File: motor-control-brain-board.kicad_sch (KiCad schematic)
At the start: 35 parts, among them J1 GPIO, J10 PWM, J11 PWR, J12 POWER_SENSE, J13 MISC_SENSE, J2 I2C, J3 SERIAL_1, J4 SERIAL_2, J5 CAN, J6 SPI, J7 USB_C_Receptacle_USB2.0_16P, J8 SWD, J9 POS_SENSE, SW1 RST, U1 TLV76750QWDRBxQ1, U2 TLV76733QWDRBxQ1

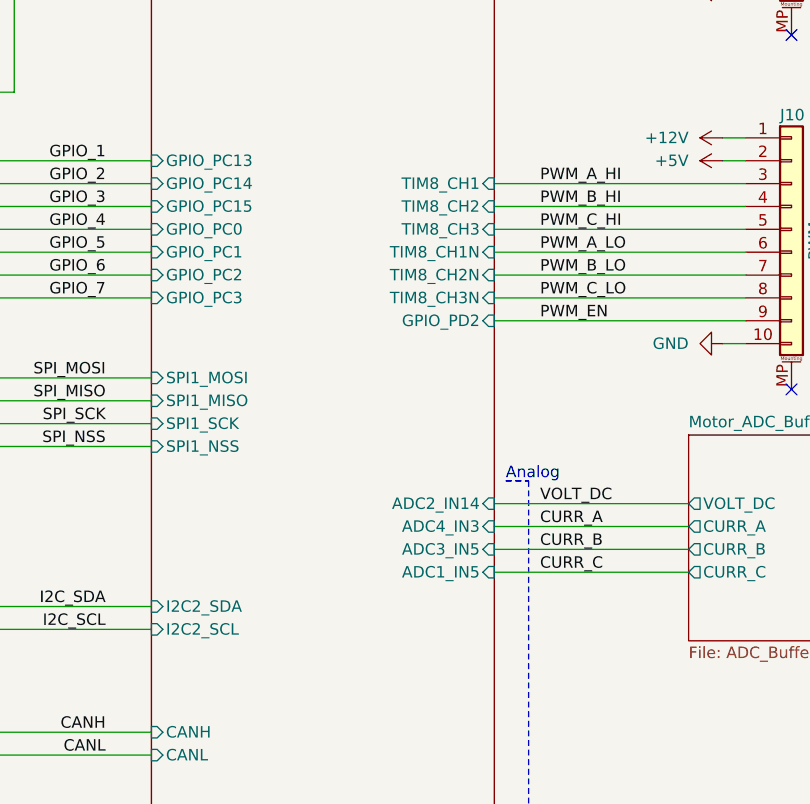
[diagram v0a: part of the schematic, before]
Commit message: Updated schematic to use HRTIM1 and reviewed
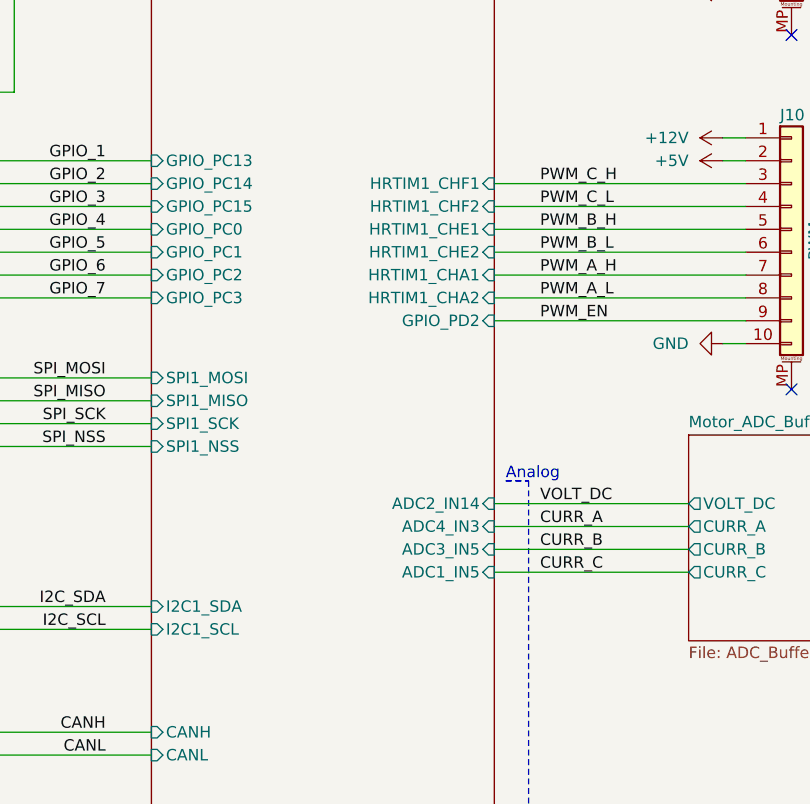
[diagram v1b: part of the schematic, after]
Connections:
- net PWM_A_HI renamed PWM_C_H
- net PWM_A_LO renamed PWM_B_L
- net PWM_B_HI renamed PWM_C_L
- net PWM_B_LO renamed PWM_A_H
- net PWM_C_HI renamed PWM_B_H
- net PWM_C_LO renamed PWM_A_L
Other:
- sheet MCU ports: added HRTIM1_CHA1, HRTIM1_CHA2, HRTIM1_CHE1, HRTIM1_CHE2, HRTIM1_CHF1, HRTIM1_CHF2, I2C1_SCL, I2C1_SDA; removed I2C2_SCL, I2C2_SDA, TIM8_CH1, TIM8_CH1N, TIM8_CH2, TIM8_CH2N, TIM8_CH3, TIM8_CH3N
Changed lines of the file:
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@@
 	(wire
 		(pts
+			(xy 137.16 78.74) (xy 165.1 78.74)
+		)
+		(stroke
+			(width 0)
+			(type default)
+		)
+	)
+	(wire
+		(pts
 			(xy 74.93 29.21) (xy 83.82 29.21)
 		)
@@
 	(wire
 		(pts
-			(xy 137.16 81.28) (xy 165.1 81.28)
-		)
-		(stroke
-			(width 0)
-			(type default)
-		)
-	)
-	(wire
-		(pts
 			(xy 74.93 21.59) (xy 81.28 21.59)
 		)
@@
 	(wire
 		(pts
+			(xy 137.16 86.36) (xy 165.1 86.36)
+		)
+		(stroke
+			(width 0)
+			(type default)
+		)
+	)
+	(wire
+		(pts
 			(xy 208.28 38.1) (xy 208.28 39.37)
 		)
@@
 		)
 	)
-	(wire
-		(pts
-			(xy 137.16 86.36) (xy 165.1 86.36)
-		)
-		(stroke
-			(width 0)
-			(type default)
-		)
-	)
 	(polyline
 		(pts
@@
 	(wire
 		(pts
-			(xy 137.16 78.74) (xy 165.1 78.74)
-		)
-		(stroke
-			(width 0)
-			(type default)
-		)
-	)
-	(wire
-		(pts
 			(xy 137.16 83.82) (xy 165.1 83.82)
 		)
@@
 	(wire
 		(pts
+			(xy 137.16 81.28) (xy 165.1 81.28)
+		)
+		(stroke
+			(width 0)
+			(type default)
+		)
+	)
+	(wire
+		(pts
 			(xy 137.16 71.12) (xy 165.1 71.12)
 		)
@@
 		)
 	)
-	(label "PWM_B_LO"
+	(label "PWM_A_H"
 		(at 142.24 81.28 0)
 		(effects
@@
 		)
 	)
-	(label "PWM_A_HI"
+	(label "PWM_C_H"
 		(at 142.24 71.12 0)
 		(effects
@@
 		)
 	)
-	(label "PWM_C_LO"
+	(label "PWM_A_L"
 		(at 142.24 83.82 0)
 		(effects
@@
 		)
 	)
-	(label "PWM_C_HI"
+	(label "PWM_B_H"
 		(at 142.24 76.2 0)
 		(effects
@@
 		)
 	)
-	(label "PWM_A_LO"
+	(label "PWM_B_L"
 		(at 142.24 78.74 0)
 		(effects
@@
 		)
 	)
-	(label "PWM_B_HI"
+	(label "PWM_C_L"
 		(at 142.24 73.66 0)
 		(effects
@@
 			)
 		)
-		(pin "TIM8_CH2N" input
-			(at 137.16 81.28 0)
-			(effects
-				(font
-					(size 1.27 1.27)
-				)
-				(justify right)
-			)
-		)
-		(pin "TIM8_CH1N" input
-			(at 137.16 78.74 0)
-			(effects
-				(font
-					(size 1.27 1.27)
-				)
-				(justify right)
-			)
-		)
-		(pin "TIM8_CH3N" input
-			(at 137.16 83.82 0)
-			(effects
-				(font
-					(size 1.27 1.27)
-				)
-				(justify right)
-			)
-		)
 		(pin "GPIO_PC15" input
 			(at 99.06 73.66 180)
@@
 			)
 		)
-		(pin "TIM8_CH3" input
-			(at 137.16 76.2 0)
-			(effects
-				(font
-					(size 1.27 1.27)
-				)
-				(justify right)
-			)
-		)
 		(pin "GPIO_PC2" input
 			(at 99.06 81.28 180)
@@
 			)
 		)
-		(pin "TIM8_CH2" input
-			(at 137.16 73.66 0)
-			(effects
-				(font
-					(size 1.27 1.27)
-				)
-				(justify right)
-			)
-		)
-		(pin "TIM8_CH1" input
-			(at 137.16 71.12 0)
-			(effects
-				(font
-					(size 1.27 1.27)
-				)
-				(justify right)
-			)
-		)
 		(pin "GPIO_PC0" input
 			(at 99.06 76.2 180)
@@
 			)
 		)
-		(pin "I2C2_SDA" input
-			(at 99.06 118.11 180)
-			(effects
-				(font
-					(size 1.27 1.27)
-				)
-				(justify left)
-			)
-		)
-		(pin "I2C2_SCL" input
-			(at 99.06 120.65 180)
-			(effects
-				(font
-					(size 1.27 1.27)
-				)
-				(justify left)
-			)
-		)
 		(pin "USB_DM" input
 			(at 99.06 44.45 180)
@@
 			)
 		)
+		(pin "HRTIM1_CHE2" input
+			(at 137.16 78.74 0)
+			(effects
+				(font
+					(size 1.27 1.27)
+				)
+				(justify right)
+			)
+		)
+		(pin "I2C1_SDA" input
+			(at 99.06 118.11 180)
+			(effects
+				(font
+					(size 1.27 1.27)
+				)
+				(justify left)
+			)
+		)
+		(pin "I2C1_SCL" input
+			(at 99.06 120.65 180)
+			(effects
+				(font
+					(size 1.27 1.27)
+				)
+				(justify left)
+			)
+		)
+		(pin "HRTIM1_CHA1" input
+			(at 137.16 81.28 0)
+			(effects
+				(font
+					(size 1.27 1.27)
+				)
+				(justify right)
+			)
+		)
+		(pin "HRTIM1_CHA2" input
+			(at 137.16 83.82 0)
+			(effects
+				(font
+					(size 1.27 1.27)
+				)
+				(justify right)
+			)
+		)
+		(pin "HRTIM1_CHE1" input
+			(at 137.16 76.2 0)
+			(effects
+				(font
+					(size 1.27 1.27)
+				)
+				(justify right)
+			)
+		)
+		(pin "HRTIM1_CHF1" input
+			(at 137.16 71.12 0)
+			(effects
+				(font
+					(size 1.27 1.27)
+				)
+				(justify right)
+			)
+		)
+		(pin "HRTIM1_CHF2" input
+			(at 137.16 73.66 0)
+			(effects
+				(font
+					(size 1.27 1.27)
+				)
+				(justify right)
+			)
+		)
 		(instances
-			(project "Motor_Control_Brain_Board"
+			(project "motor-control-brain-board"
 				(path "/7261d109-8405-40e9-921c-d95f374a7164"
 					(page "2")
@@
 		)
 		(instances
-			(project "Motor_Control_Brain_Board"
+			(project "motor-control-brain-board"
 				(path "/7261d109-8405-40e9-921c-d95f374a7164"
 					(page "4")
@@
 		)
 		(instances
-			(project "Motor_Control_Brain_Board"
+			(project "motor-control-brain-board"
 				(path "/7261d109-8405-40e9-921c-d95f374a7164"
 					(page "3")

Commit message: Routed Stuff
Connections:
- net CANH: now also J5.3 (Pin_3); no longer J5.2 (Pin_2)
- net CANL: now also J5.2 (Pin_2); no longer J5.3 (Pin_3)
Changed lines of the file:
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@@
 	(wire
 		(pts
+			(xy 60.96 134.62) (xy 99.06 134.62)
+		)
+		(stroke
+			(width 0)
+			(type default)
+		)
+	)
+	(wire
+		(pts
 			(xy 208.28 26.67) (xy 208.28 27.94)
 		)
@@
 	(wire
 		(pts
-			(xy 60.96 134.62) (xy 99.06 134.62)
-		)
-		(stroke
-			(width 0)
-			(type default)
-		)
-	)
-	(wire
-		(pts
 			(xy 191.77 106.68) (xy 217.17 106.68)
 		)
@@
 	(wire
 		(pts
+			(xy 60.96 132.08) (xy 99.06 132.08)
+		)
+		(stroke
+			(width 0)
+			(type default)
+		)
+	)
+	(wire
+		(pts
 			(xy 191.77 119.38) (xy 217.17 119.38)
 		)
@@
 	(wire
 		(pts
-			(xy 60.96 132.08) (xy 99.06 132.08)
-		)
-		(stroke
-			(width 0)
-			(type default)
-		)
-	)
-	(wire
-		(pts
 			(xy 242.57 64.77) (xy 234.95 64.77)
 		)
@@
 	)
 	(label "CANL"
-		(at 93.98 134.62 180)
+		(at 93.98 132.08 180)
 		(effects
 			(font
@@
 	)
 	(label "CANH"
-		(at 93.98 132.08 180)
+		(at 93.98 134.62 180)
 		(effects
 			(font
@@
 		)
 		(pin "CANH" input
-			(at 99.06 132.08 180)
+			(at 99.06 134.62 180)
 			(effects
 				(font
@@
 		)
 		(pin "CANL" input
-			(at 99.06 134.62 180)
+			(at 99.06 132.08 180)
 			(effects
 				(font

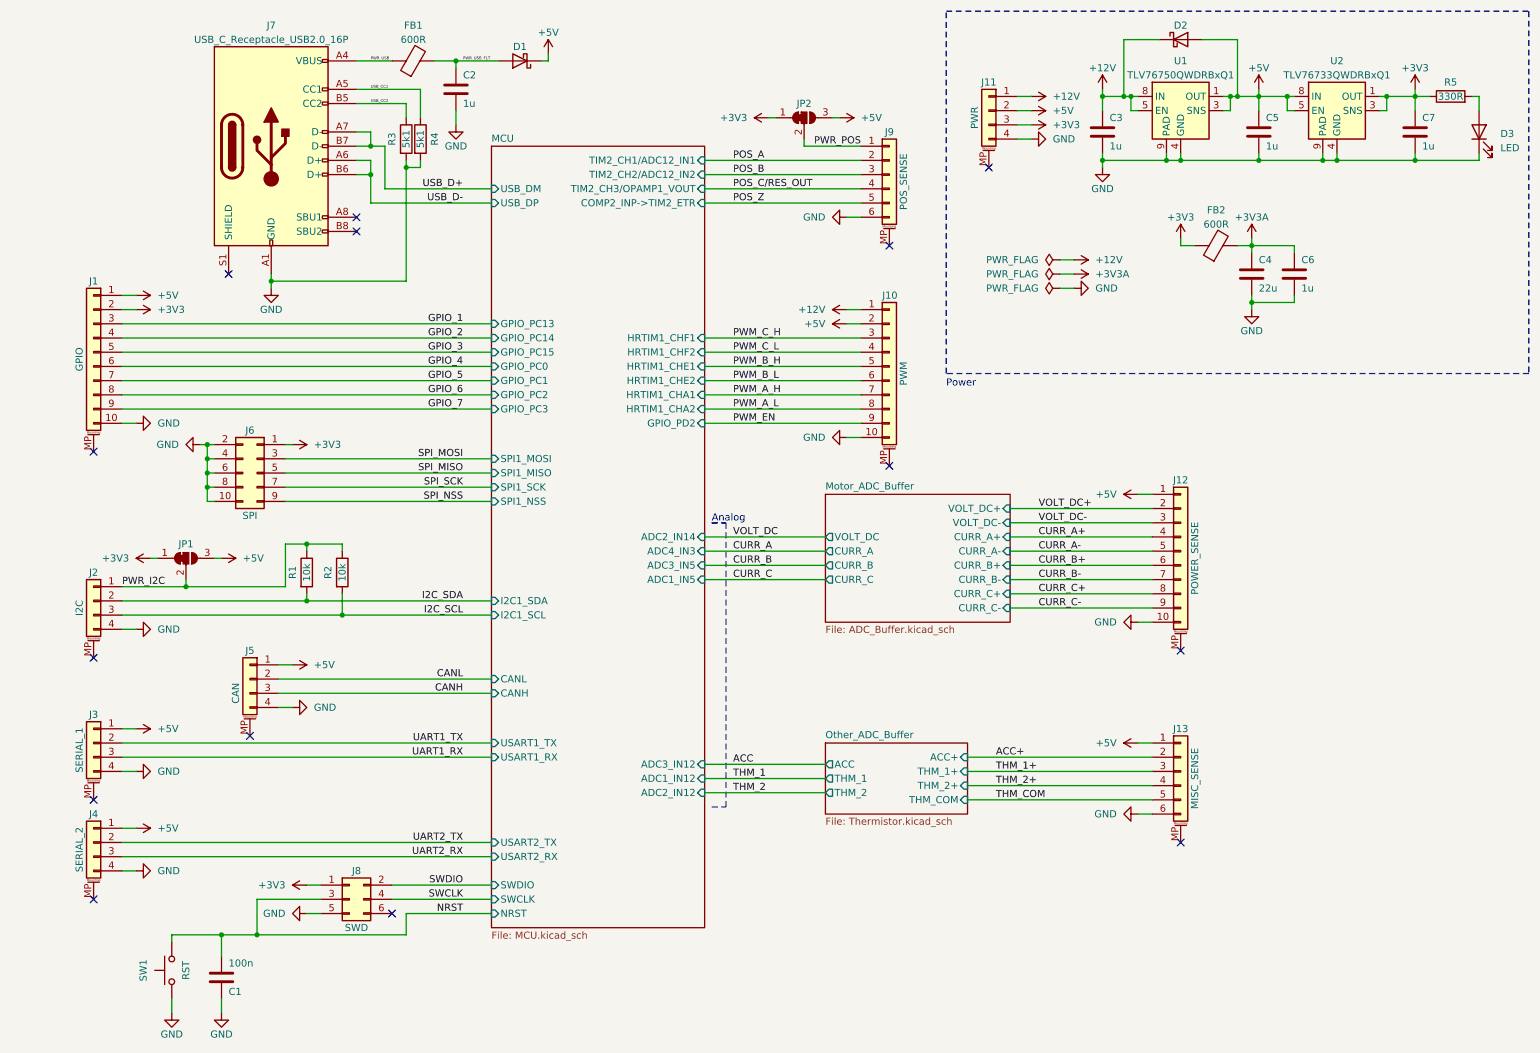
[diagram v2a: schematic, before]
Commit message: Continued work on PCB layout, think I should add castellated holes as an alternative to connectors
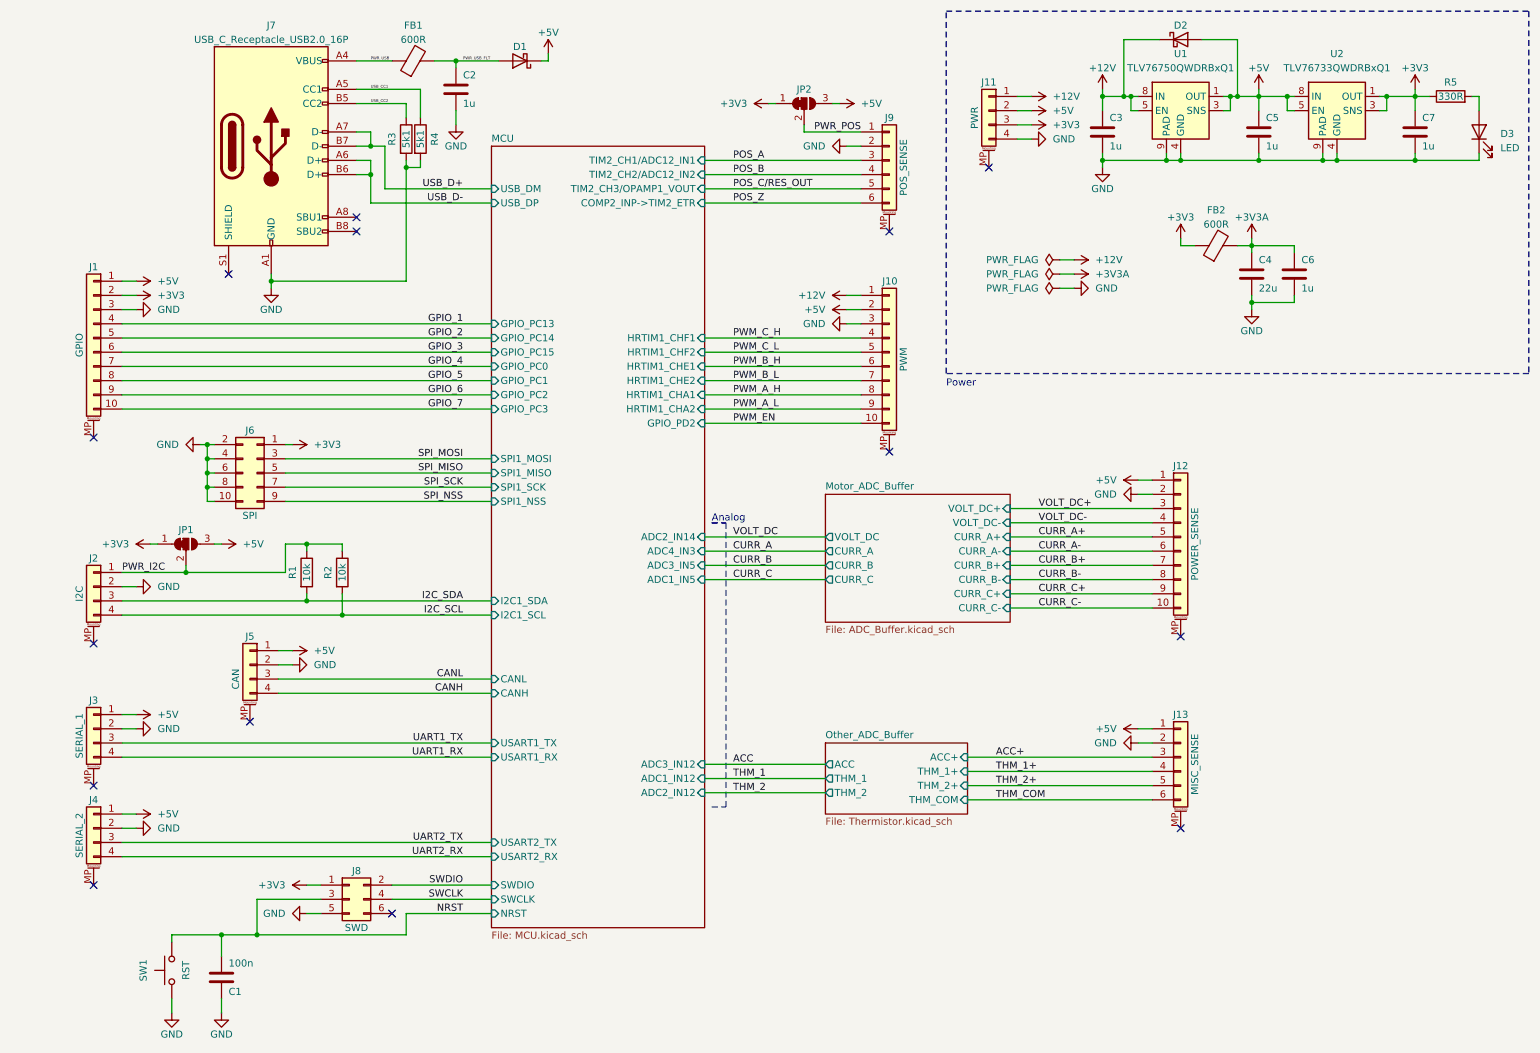
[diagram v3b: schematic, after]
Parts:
- U1, U2: footprint Package_SON:VSON-8-1EP_3x3mm_P0.65mm_EP1.65x2.4mm_ThermalVias -> Package_SON:VSON-8-1EP_3x3mm_P0.65mm_EP1.65x2.4mm
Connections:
- net ACC+: now also J13.3 (Pin_3); no longer J13.2 (Pin_2)
- net CANH: now also J5.4 (Pin_4); no longer J5.3 (Pin_3)
- net CANL: now also J5.3 (Pin_3); no longer J5.2 (Pin_2)
- net CURR_A+: now also J12.5 (Pin_5); no longer J12.4 (Pin_4)
- net CURR_A-: now also J12.6 (Pin_6); no longer J12.5 (Pin_5)
- net CURR_B+: now also J12.7 (Pin_7); no longer J12.6 (Pin_6)
- net CURR_B-: now also J12.8 (Pin_8); no longer J12.7 (Pin_7)
- net CURR_C+: now also J12.9 (Pin_9); no longer J12.8 (Pin_8)
- net CURR_C-: now also J12.10 (Pin_10); no longer J12.9 (Pin_9)
- net GND: now also J1.3 (Pin_3), J10.3 (Pin_3), J12.2 (Pin_2), J13.2 (Pin_2), J2.2 (Pin_2), J3.2 (Pin_2), J4.2 (Pin_2), J5.2 (Pin_2), J9.2 (Pin_2); no longer J1.10 (Pin_10), J10.10 (Pin_10), J12.10 (Pin_10), J13.6 (Pin_6), J2.4 (Pin_4), J3.4 (Pin_4), J4.4 (Pin_4), J5.4 (Pin_4), J9.6 (Pin_6)
- net GPIO_1: now also J1.4 (Pin_4); no longer J1.3 (Pin_3)
- net GPIO_2: now also J1.5 (Pin_5); no longer J1.4 (Pin_4)
- net GPIO_3: now also J1.6 (Pin_6); no longer J1.5 (Pin_5)
- net GPIO_4: now also J1.7 (Pin_7); no longer J1.6 (Pin_6)
- net GPIO_5: now also J1.8 (Pin_8); no longer J1.7 (Pin_7)
- net GPIO_6: now also J1.9 (Pin_9); no longer J1.8 (Pin_8)
- net GPIO_7: now also J1.10 (Pin_10); no longer J1.9 (Pin_9)
- net I2C_SCL: now also J2.4 (Pin_4); no longer J2.3 (Pin_3)
- net I2C_SDA: now also J2.3 (Pin_3); no longer J2.2 (Pin_2)
- net POS_A: now also J9.3 (Pin_3); no longer J9.2 (Pin_2)
- net POS_B: now also J9.4 (Pin_4); no longer J9.3 (Pin_3)
- net POS_C/RES_OUT: now also J9.5 (Pin_5); no longer J9.4 (Pin_4)
- net POS_Z: now also J9.6 (Pin_6); no longer J9.5 (Pin_5)
- net PWM_A_H: now also J10.8 (Pin_8); no longer J10.7 (Pin_7)
- net PWM_A_L: now also J10.9 (Pin_9); no longer J10.8 (Pin_8)
- net PWM_B_H: now also J10.6 (Pin_6); no longer J10.5 (Pin_5)
- net PWM_B_L: now also J10.7 (Pin_7); no longer J10.6 (Pin_6)
- net PWM_C_H: now also J10.4 (Pin_4); no longer J10.3 (Pin_3)
- net PWM_C_L: now also J10.5 (Pin_5); no longer J10.4 (Pin_4)
- net PWM_EN: now also J10.10 (Pin_10); no longer J10.9 (Pin_9)
- net THM_1+: now also J13.4 (Pin_4); no longer J13.3 (Pin_3)
- net THM_2+: now also J13.5 (Pin_5); no longer J13.4 (Pin_4)
- net THM_COM: now also J13.6 (Pin_6); no longer J13.5 (Pin_5)
- net UART1_RX: now also J3.4 (Pin_4); no longer J3.3 (Pin_3)
- net UART1_TX: now also J3.3 (Pin_3); no longer J3.2 (Pin_2)
- net UART2_RX: now also J4.4 (Pin_4); no longer J4.3 (Pin_3)
- net UART2_TX: now also J4.3 (Pin_3); no longer J4.2 (Pin_2)
- net VOLT_DC+: now also J12.3 (Pin_3); no longer J12.2 (Pin_2)
- net VOLT_DC-: now also J12.4 (Pin_4); no longer J12.3 (Pin_3)
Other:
- moved on the sheet: J1, J10, J12, J13, J2, J3, J4, J5, J9, JP1, JP2
